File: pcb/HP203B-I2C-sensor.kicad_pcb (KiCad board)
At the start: 2 copper layers, 18 x 26 mm, 11 parts, among them J1 Conn_01x04_Socket, J2 Conn_01x04_Pin, J3 Conn_01x04_Socket

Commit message: polish a bit
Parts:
- C1: value 4.1u -> 4.7u
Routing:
- net GND: vias 0 -> 8
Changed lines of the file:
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@@
 	(generator_version "10.0")
 	(general
-		(thickness 1.6)
+		(thickness 1.659981)
 		(legacy_teardrops no)
 	)
@@
 		(17 "Dwgs.User" user "User.Drawings")
 		(19 "Cmts.User" user "User.Comments")
-		(21 "Eco1.User" user "User.Eco1")
-		(23 "Eco2.User" user "User.Eco2")
 		(25 "Edge.Cuts" user)
 		(27 "Margin" user)
@@
 		(35 "F.Fab" user)
 		(33 "B.Fab" user)
-		(39 "User.1" user)
-		(41 "User.2" user)
-		(43 "User.3" user)
-		(45 "User.4" user)
 	)
 	(setup
+		(stackup
+			(layer "F.SilkS"
+				(type "Top Silk Screen")
+			)
+			(layer "F.Paste"
+				(type "Top Solder Paste")
+			)
+			(layer "F.Mask"
+				(type "Top Solder Mask")
+				(thickness 0.01)
+			)
+			(layer "F.Cu"
+				(type "copper")
+				(thickness 0.035)
+			)
+			(layer "dielectric 1"
+				(type "core")
+				(thickness 1.569981)
+				(material "FR4")
+				(epsilon_r 4.2)
+				(loss_tangent 0.02)
+			)
+			(layer "B.Cu"
+				(type "copper")
+				(thickness 0.035)
+			)
+			(layer "B.Mask"
+				(type "Bottom Solder Mask")
+				(thickness 0.01)
+			)
+			(layer "B.Paste"
+				(type "Bottom Solder Paste")
+			)
+			(layer "B.SilkS"
+				(type "Bottom Silk Screen")
+			)
+			(copper_finish "None")
+			(dielectric_constraints no)
+		)
 		(pad_to_mask_clearance 0)
-		(allow_soldermask_bridges_in_footprints no)
+		(allow_soldermask_bridges_in_footprints yes)
 		(tenting
 			(front yes)
@@
 			(outputformat 1)
 			(mirror no)
-			(drillshape 1)
+			(drillshape 0)
 			(scaleselection 1)
-			(outputdirectory "")
+			(outputdirectory "gerber/")
 		)
 	)
@@
 				(font
 					(size 1.27 1.27)
+					(thickness 0.15)
 				)
 			)
@@
 				(font
 					(size 1.27 1.27)
+					(thickness 0.15)
 				)
 			)
@@
 			)
 		)
-		(property "Value" "4.1u"
+		(property "Value" "4.7u"
 			(at 0 1.16 90)
 			(layer "F.Fab")
@@
 	)
 	(segment
+		(start 148.7 114.32)
+		(end 150.1709 114.32)
+		(width 0.2)
+		(layer "F.Cu")
+		(net "GND")
+	)
+	(segment
+		(start 150.1709 114.32)
+		(end 150.2002 114.3493)
+		(width 0.2)
+		(layer "F.Cu")
+		(net "GND")
+	)
+	(via
+		(at 146.6 122)
+		(size 0.6)
+		(drill 0.3)
+		(layers "F.Cu" "B.Cu")
+		(free yes)
+		(net "GND")
+	)
+	(via
+		(at 155.1 122.7)
+		(size 0.6)
+		(drill 0.3)
+		(layers "F.Cu" "B.Cu")
+		(free yes)
+		(net "GND")
+	)
+	(via
+		(at 155.2 119.2)
+		(size 0.6)
+		(drill 0.3)
+		(layers "F.Cu" "B.Cu")
+		(free yes)
+		(net "GND")
+	)
+	(via
+		(at 146.2 119)
+		(size 0.6)
+		(drill 0.3)
+		(layers "F.Cu" "B.Cu")
+		(free yes)
+		(net "GND")
+	)
+	(via
+		(at 155.1 104.9)
+		(size 0.6)
+		(drill 0.3)
+		(layers "F.Cu" "B.Cu")
+		(free yes)
+		(net "GND")
+	)
+	(via
+		(at 155.1 108.8)
+		(size 0.6)
+		(drill 0.3)
+		(layers "F.Cu" "B.Cu")
+		(free yes)
+		(net "GND")
+	)
+	(via
+		(at 146.9 104.9)
+		(size 0.6)
+		(drill 0.3)
+		(layers "F.Cu" "B.Cu")
+		(free yes)
+		(net "GND")
+	)
+	(via
+		(at 151.3 111.8)
+		(size 0.6)
+		(drill 0.3)
+		(layers "F.Cu" "B.Cu")
+		(free yes)
+		(net "GND")
+	)
+	(segment
 		(start 154.6 113.3)
 		(end 153.1499 113.3)
@@
 	)
 	(segment
-		(start 148.7 114.32)
-		(end 150.1709 114.32)
-		(width 0.2)
-		(layer "F.Cu")
-		(net "GND")
-	)
-	(segment
-		(start 150.1709 114.32)
-		(end 150.2002 114.3493)
-		(width 0.2)
-		(layer "F.Cu")
-		(net "GND")
-	)
-	(segment
 		(start 155.6 116.3)
 		(end 155.6 115.4)
@@
 		(layers "F.Cu" "B.Cu")
 		(hatch edge 0.5)
-		(connect_pads
+		(connect_pads yes
 			(clearance 0.5)
 		)

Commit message: add pinout names and do other cosmetic changes
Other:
- board text added: "SCL SDA VCC GND"
- board text added: "riscfruit.com"
- board text removed: "riscfruit.net"

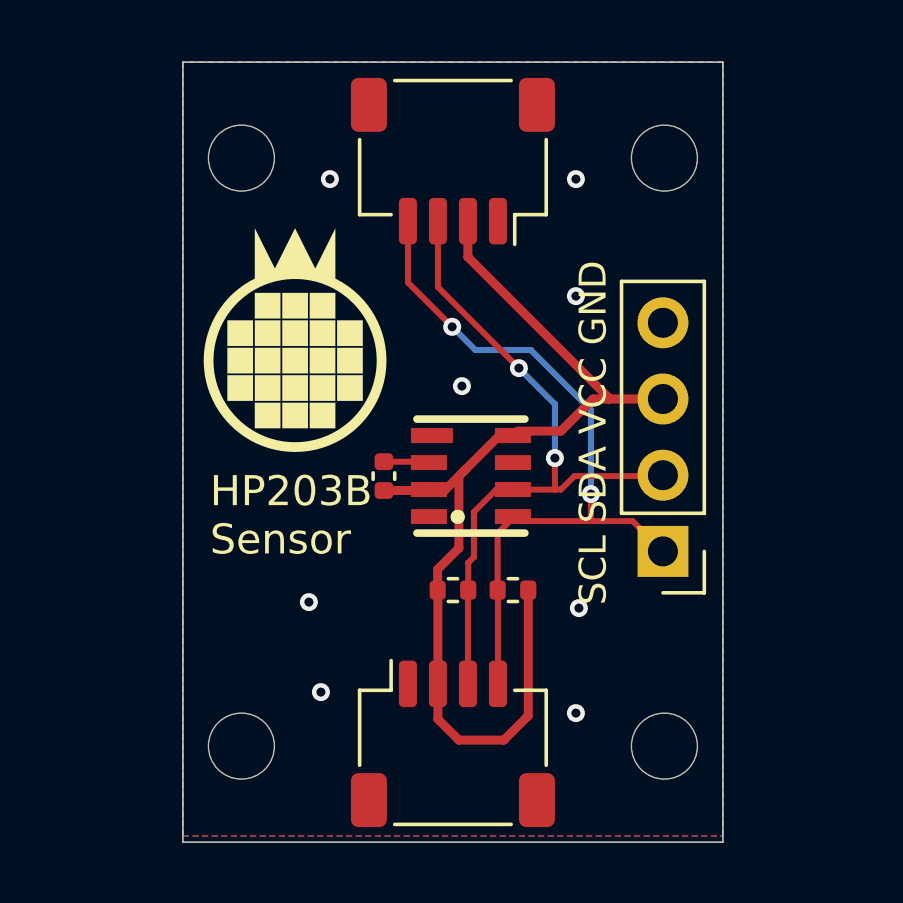
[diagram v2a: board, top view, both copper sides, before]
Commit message: change shape to 26x26mm square
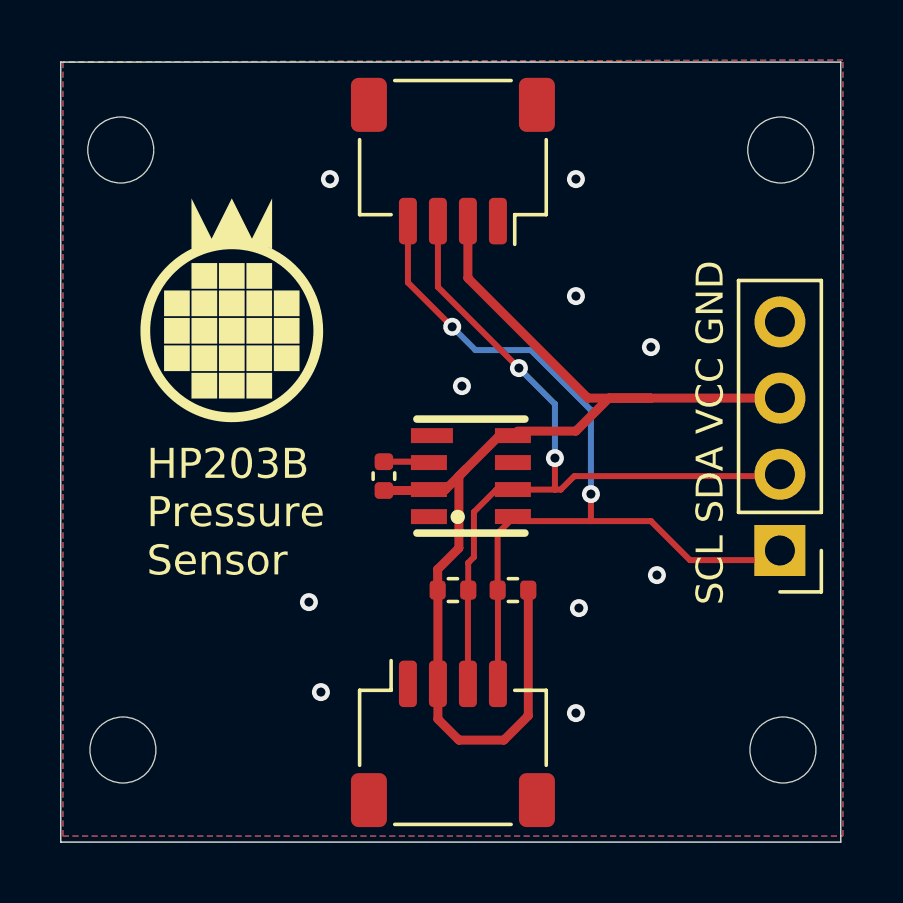
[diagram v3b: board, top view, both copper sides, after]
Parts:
- removed the H1 at (158.1, 123.8)
- removed the H1 at (158.1, 104.2)
- removed the H1 at (143.9, 104.2)
- removed the H1 at (143.9, 123.8)
- added H1: MountingHole, MountingHole:MountingHole_2.2mm_M2, F.Cu at (162.0, 123.9)
- added H1: MountingHole, MountingHole:MountingHole_2.2mm_M2, F.Cu at (161.9, 103.9)
- added H1: MountingHole, MountingHole:MountingHole_2.2mm_M2, F.Cu at (139.9, 103.9)
- added H1: MountingHole, MountingHole:MountingHole_2.2mm_M2, F.Cu at (140.0, 123.9)
- moved J2 3.90 mm to (161.9, 117.3)
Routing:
- net +3.3V: track 34.7 -> 40.4 mm
- net /SCL: track 24.9 -> 29.0 mm
- net /SDA: track 23.0 -> 26.9 mm
- net GND: vias 8 -> 10
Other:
- board size 18 x 26 mm -> 26 x 26 mm
- board text added: "HP203B Pressure Sensor"
- board text removed: "HP203B Sensor"
